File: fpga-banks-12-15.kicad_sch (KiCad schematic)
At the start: 1 part, among them U1 XC7K410T-2FFG900I

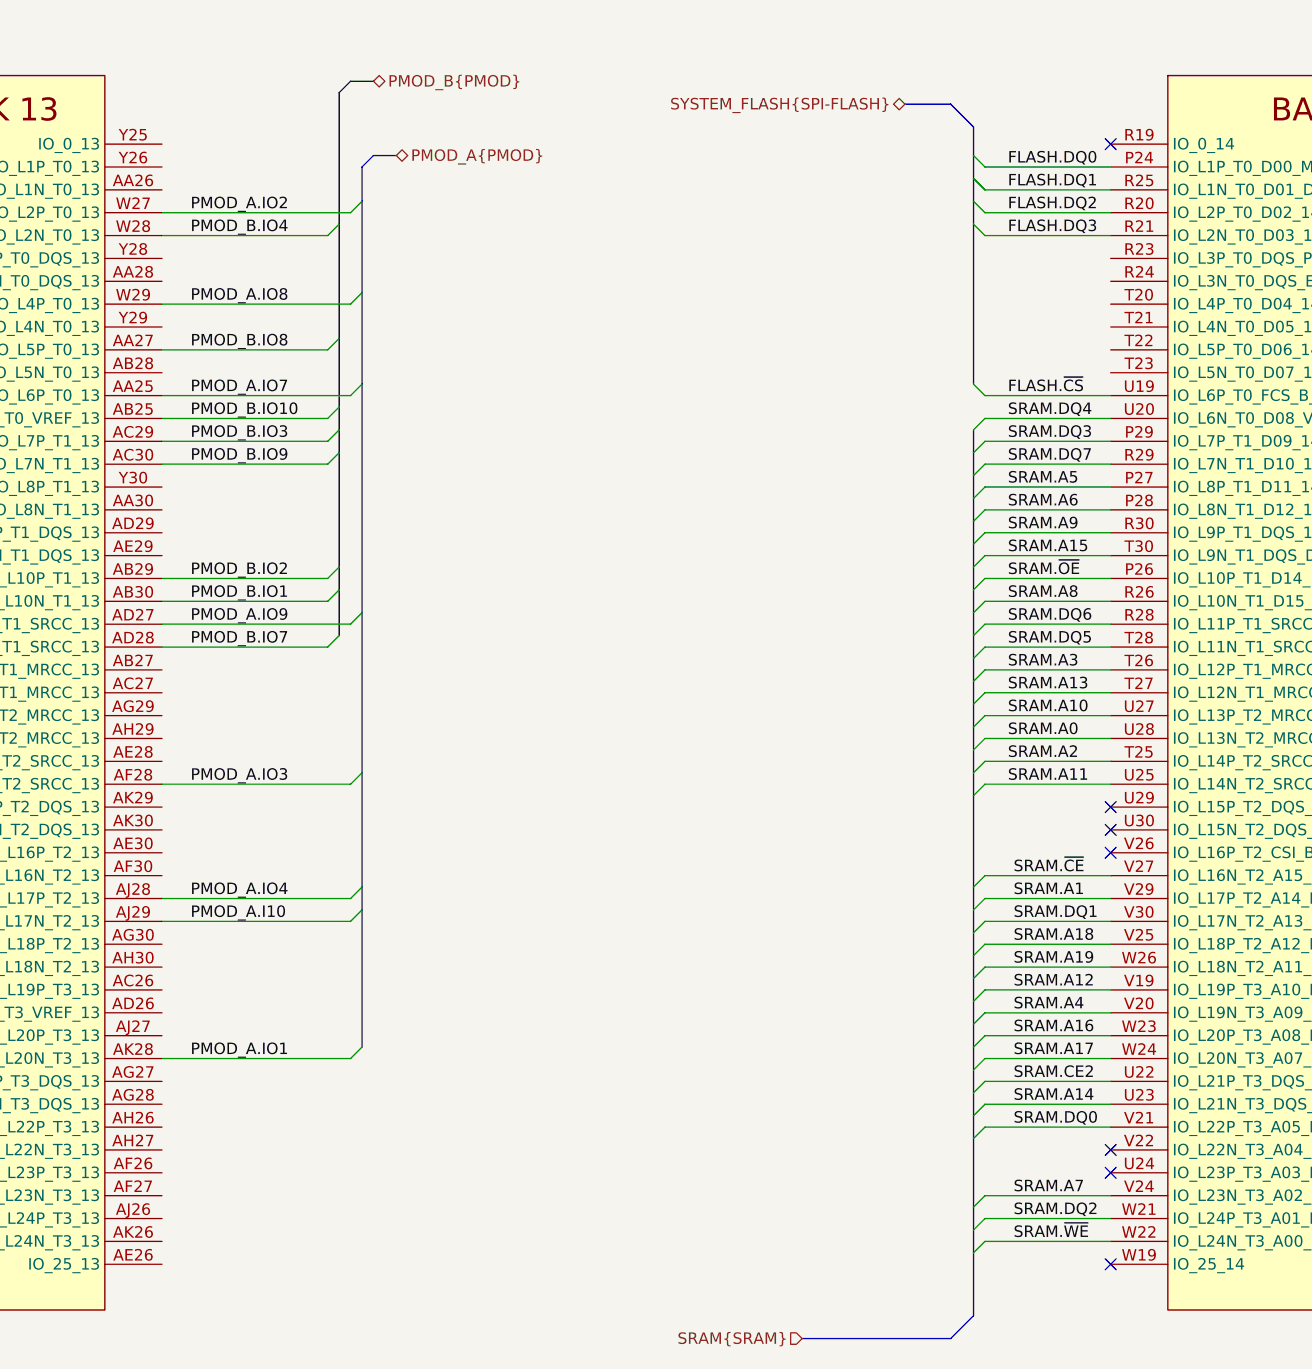
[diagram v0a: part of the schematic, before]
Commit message: Update system flash bus unfolded labels
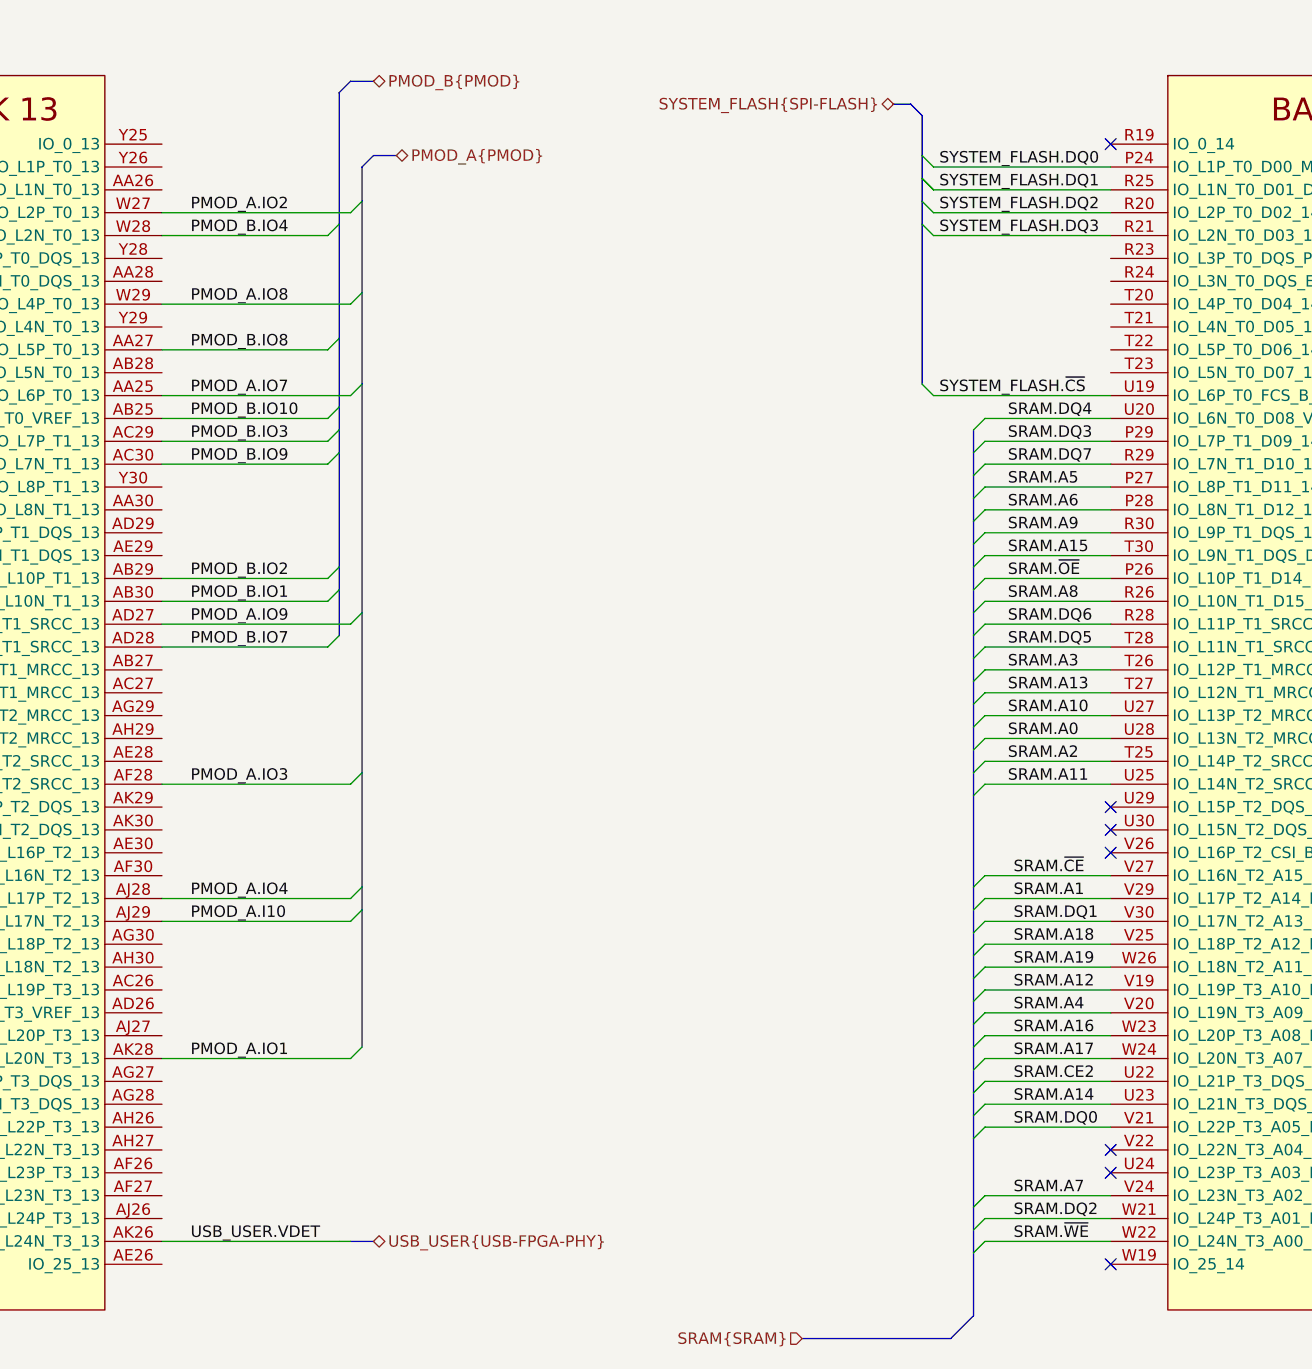
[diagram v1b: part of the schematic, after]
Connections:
- net USB_USER.VDET: now reaches U1.AK26 (IO_L24N_T3_13)
- net FLASH.DQ0 renamed SYSTEM_FLASH.DQ0
- net FLASH.DQ1 renamed SYSTEM_FLASH.DQ1
- net FLASH.DQ2 renamed SYSTEM_FLASH.DQ2
- net FLASH.DQ3 renamed SYSTEM_FLASH.DQ3
- net FLASH.~{CS} renamed SYSTEM_FLASH.~{CS}
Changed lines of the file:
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@@
     (stroke (width 0) (type default) (color 0 0 0 0))
   )
-  (bus_entry (at 240.03 80.01) (size 1.27 1.27)
+  (bus_entry (at 234.315 80.01) (size 1.27 1.27)
     (stroke (width 0) (type default) (color 0 0 0 0))
   )
@@
     (stroke (width 0) (type default) (color 0 0 0 0))
   )
-  (bus_entry (at 240.03 80.01) (size 1.27 1.27)
+  (bus_entry (at 234.315 80.01) (size 1.27 1.27)
     (stroke (width 0) (type default) (color 0 0 0 0))
   )
@@
     (stroke (width 0) (type default) (color 0 0 0 0))
   )
-  (bus_entry (at 240.03 102.87) (size 1.27 1.27)
-    (stroke (width 0) (type default) (color 0 0 0 0))
-  )
-  (bus_entry (at 240.03 77.47) (size 1.27 1.27)
+  (bus_entry (at 234.315 102.87) (size 1.27 1.27)
+    (stroke (width 0) (type default) (color 0 0 0 0))
+  )
+  (bus_entry (at 234.315 77.47) (size 1.27 1.27)
     (stroke (width 0) (type default) (color 0 0 0 0))
   )
@@
     (stroke (width 0) (type default) (color 0 0 0 0))
   )
-  (bus_entry (at 240.03 85.09) (size 1.27 1.27)
+  (bus_entry (at 234.315 85.09) (size 1.27 1.27)
     (stroke (width 0) (type default) (color 0 0 0 0))
   )
@@
     (stroke (width 0) (type default) (color 0 0 0 0))
   )
+  (bus_entry (at 169.545 198.12) (size 1.27 0)
+    (stroke (width 0) (type default) (color 0 0 0 0))
+  )
   (bus_entry (at 172.085 158.75) (size -1.27 1.27)
     (stroke (width 0) (type default) (color 0 0 0 0))
@@
     (stroke (width 0) (type default) (color 0 0 0 0))
   )
-  (bus_entry (at 240.03 82.55) (size 1.27 1.27)
+  (bus_entry (at 234.315 82.55) (size 1.27 1.27)
     (stroke (width 0) (type default) (color 0 0 0 0))
   )
@@
     (stroke (width 0) (type default) (color 0 0 0 0))
   )
-  (wire (pts (xy 241.3 78.74) (xy 255.27 78.74))
+  (wire (pts (xy 235.585 78.74) (xy 255.27 78.74))
     (stroke (width 0) (type default) (color 0 0 0 0))
   )
@@
     (stroke (width 0) (type default) (color 0 0 0 0))
   )
-  (bus (pts (xy 232.41 71.755) (xy 237.49 71.755))
-    (stroke (width 0) (type default) (color 0 0 0 0))
-  )
   (wire (pts (xy 241.3 139.7) (xy 255.27 139.7))
     (stroke (width 0) (type default) (color 0 0 0 0))
@@
     (stroke (width 0) (type default) (color 0 0 0 0))
   )
-  (bus (pts (xy 240.03 85.09) (xy 240.03 102.87))
+  (bus (pts (xy 234.315 85.09) (xy 234.315 102.87))
     (stroke (width 0) (type default) (color 0 0 0 0))
   )
@@
     (stroke (width 0) (type default) (color 0 0 0 0))
   )
-  (wire (pts (xy 241.3 104.14) (xy 255.27 104.14))
+  (wire (pts (xy 235.585 104.14) (xy 255.27 104.14))
     (stroke (width 0) (type default) (color 0 0 0 0))
   )
@@
     (stroke (width 0) (type default) (color 0 0 0 0))
   )
-  (wire (pts (xy 241.3 83.82) (xy 255.27 83.82))
+  (wire (pts (xy 235.585 83.82) (xy 255.27 83.82))
     (stroke (width 0) (type default) (color 0 0 0 0))
   )
@@
     (stroke (width 0) (type default) (color 0 0 0 0))
   )
-  (wire (pts (xy 241.3 86.36) (xy 255.27 86.36))
+  (wire (pts (xy 235.585 86.36) (xy 255.27 86.36))
     (stroke (width 0) (type default) (color 0 0 0 0))
   )
@@
     (stroke (width 0) (type default) (color 0 0 0 0))
   )
+  (bus (pts (xy 233.045 71.755) (xy 231.14 71.755))
+    (stroke (width 0) (type default) (color 0 0 0 0))
+  )
   (wire (pts (xy 241.3 127) (xy 255.27 127))
     (stroke (width 0) (type default) (color 0 0 0 0))
@@
     (stroke (width 0) (type default) (color 0 0 0 0))
   )
-  (bus (pts (xy 240.03 74.295) (xy 240.03 77.47))
+  (wire (pts (xy 169.545 198.12) (xy 149.86 198.12))
+    (stroke (width 0) (type default) (color 0 0 0 0))
+  )
+  (bus (pts (xy 234.315 73.025) (xy 234.315 77.47))
     (stroke (width 0) (type default) (color 0 0 0 0))
   )
@@
     (stroke (width 0) (type default) (color 0 0 0 0))
   )
-  (bus (pts (xy 237.49 71.755) (xy 240.03 74.295))
-    (stroke (width 0) (type default) (color 0 0 0 0))
-  )
   (bus (pts (xy 240.03 110.49) (xy 240.03 113.03))
     (stroke (width 0) (type default) (color 0 0 0 0))
@@
     (stroke (width 0) (type default) (color 0 0 0 0))
   )
+  (bus (pts (xy 234.315 73.025) (xy 233.045 71.755))
+    (stroke (width 0) (type default) (color 0 0 0 0))
+  )
   (bus (pts (xy 172.085 82.55) (xy 172.085 92.71))
     (stroke (width 0) (type default) (color 0 0 0 0))
@@
     (stroke (width 0) (type default) (color 0 0 0 0))
   )
-  (bus (pts (xy 240.03 77.47) (xy 240.03 80.01))
+  (bus (pts (xy 234.315 77.47) (xy 234.315 80.01))
     (stroke (width 0) (type default) (color 0 0 0 0))
   )
@@
     (stroke (width 0) (type default) (color 0 0 0 0))
   )
+  (bus (pts (xy 170.815 198.12) (xy 173.355 198.12))
+    (stroke (width 0) (type default) (color 0 0 0 0))
+  )
   (wire (pts (xy 149.86 109.22) (xy 168.275 109.22))
     (stroke (width 0) (type default) (color 0 0 0 0))
@@
     (stroke (width 0) (type default) (color 0 0 0 0))
   )
-  (wire (pts (xy 241.3 81.28) (xy 255.27 81.28))
+  (wire (pts (xy 235.585 81.28) (xy 255.27 81.28))
     (stroke (width 0) (type default) (color 0 0 0 0))
   )
@@
     (stroke (width 0) (type default) (color 0 0 0 0))
   )
-  (bus (pts (xy 240.03 80.01) (xy 240.03 82.55))
+  (bus (pts (xy 234.315 80.01) (xy 234.315 82.55))
     (stroke (width 0) (type default) (color 0 0 0 0))
   )
@@
     (stroke (width 0) (type default) (color 0 0 0 0))
   )
-  (bus (pts (xy 240.03 82.55) (xy 240.03 85.09))
+  (bus (pts (xy 234.315 82.55) (xy 234.315 85.09))
     (stroke (width 0) (type default) (color 0 0 0 0))
   )
@@
     (effects (font (size 1.27 1.27)) (justify left bottom))
   )
-  (label "FLASH.DQ0" (at 243.84 78.74 0)
+  (label "SYSTEM_FLASH.DQ0" (at 236.22 78.74 0)
     (effects (font (size 1.27 1.27)) (justify left bottom))
   )
@@
     (effects (font (size 1.27 1.27)) (justify left bottom))
   )
+  (label "USB_USER.VDET" (at 153.035 198.12 0)
+    (effects (font (size 1.27 1.27)) (justify left bottom))
+  )
   (label "SRAM.DQ3" (at 243.84 109.22 0)
     (effects (font (size 1.27 1.27)) (justify left bottom))
   )
-  (label "FLASH.DQ2" (at 243.84 83.82 0)
+  (label "SYSTEM_FLASH.DQ2" (at 236.22 83.82 0)
     (effects (font (size 1.27 1.27)) (justify left bottom))
   )
@@
     (effects (font (size 1.27 1.27)) (justify left bottom))
   )
-  (label "FLASH.~{CS}" (at 243.84 104.14 0)
+  (label "SYSTEM_FLASH.~{CS}" (at 236.22 104.14 0)
     (effects (font (size 1.27 1.27)) (justify left bottom))
   )
@@
     (effects (font (size 1.27 1.27)) (justify left bottom))
   )
-  (label "FLASH.DQ1" (at 243.84 81.28 0)
+  (label "SYSTEM_FLASH.DQ1" (at 236.22 81.28 0)
     (effects (font (size 1.27 1.27)) (justify left bottom))
   )
@@
     (effects (font (size 1.27 1.27)) (justify left bottom))
   )
-  (label "FLASH.DQ3" (at 243.84 86.36 0)
+  (label "SYSTEM_FLASH.DQ3" (at 236.22 86.36 0)
     (effects (font (size 1.27 1.27)) (justify left bottom))
   )
@@
     (effects (font (size 1.27 1.27)) (justify left bottom))
   )
-  (hierarchical_label "SYSTEM_FLASH{SPI-FLASH}" (shape bidirectional) (at 232.41 71.755 180)
+  (hierarchical_label "USB_USER{USB-FPGA-PHY}" (shape bidirectional) (at 173.355 198.12 0)
+    (effects (font (size 1.27 1.27)) (justify left))
+  )
+  (hierarchical_label "SYSTEM_FLASH{SPI-FLASH}" (shape bidirectional) (at 231.14 71.755 180)
     (effects (font (size 1.27 1.27)) (justify right))
   )

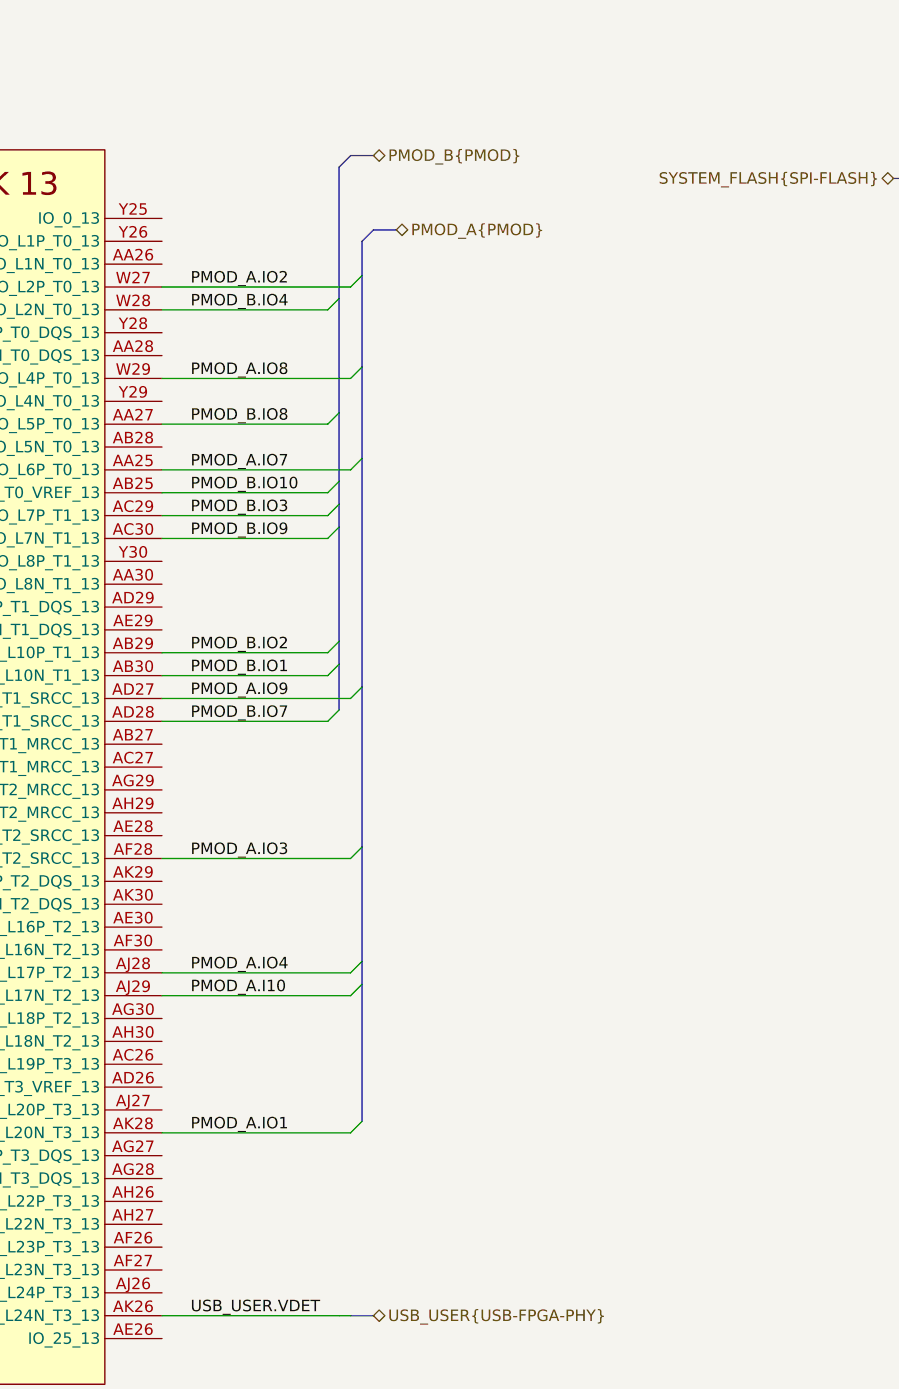
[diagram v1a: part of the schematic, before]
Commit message: Connect LED, DIP switch and buttons to FPGA
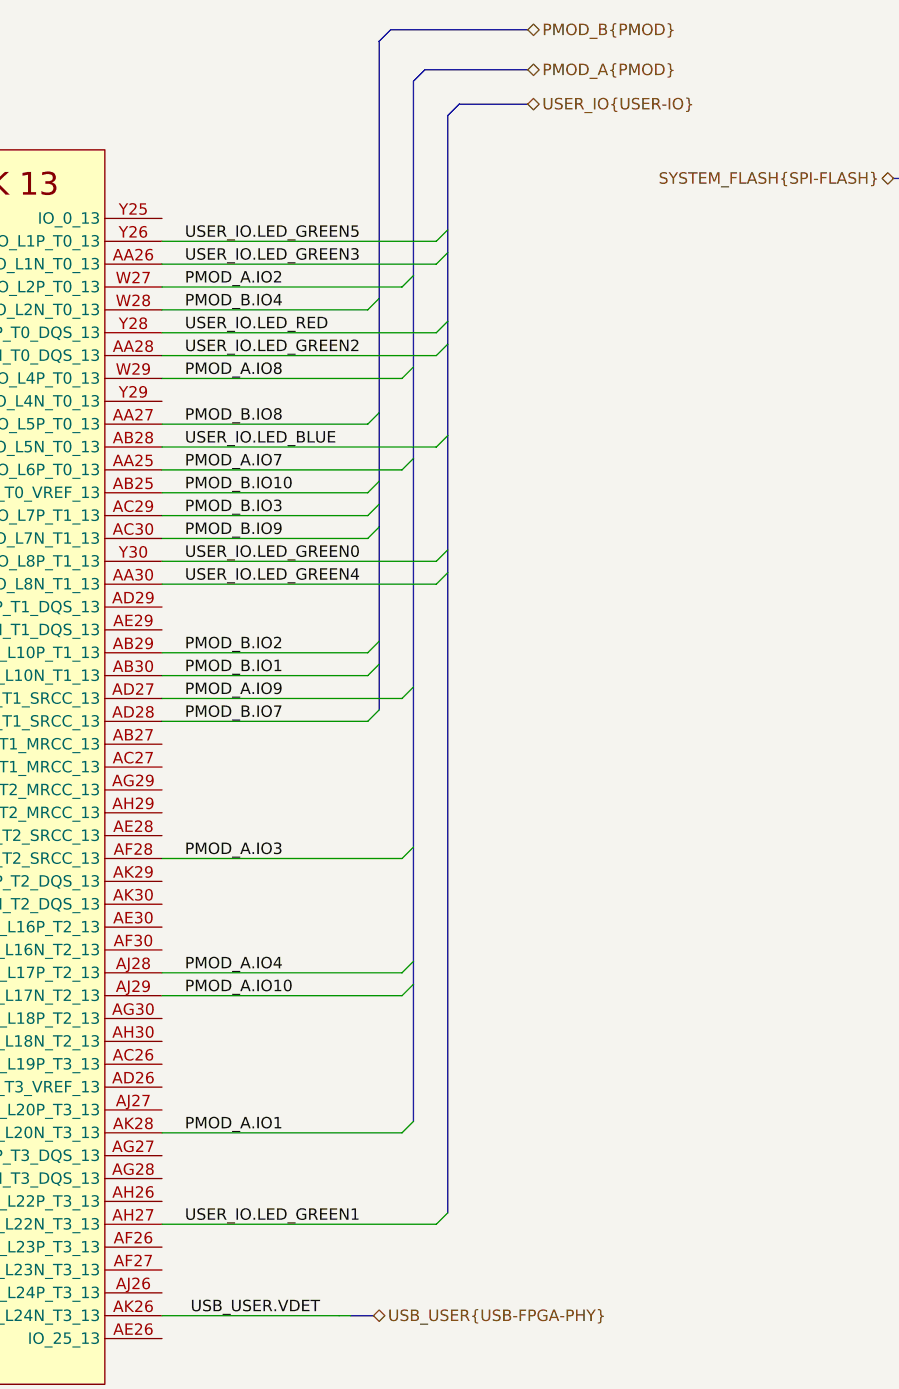
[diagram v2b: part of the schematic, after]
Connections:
- net USER_IO.LED_GREEN3: now reaches U1.AA26 (IO_L1N_T0_13)
- net USER_IO.LED_GREEN2: now reaches U1.AA28 (IO_L3N_T0_DQS_13)
- net USER_IO.LED_GREEN4: now reaches U1.AA30 (IO_L8N_T1_13)
- net USER_IO.LED_BLUE: now reaches U1.AB28 (IO_L5N_T0_13)
- net USER_IO.LED_GREEN1: now reaches U1.AH27 (IO_L22N_T3_13)
- net USER_IO.LED_GREEN5: now reaches U1.Y26 (IO_L1P_T0_13)
- net USER_IO.LED_RED: now reaches U1.Y28 (IO_L3P_T0_DQS_13)
- net USER_IO.LED_GREEN0: now reaches U1.Y30 (IO_L8P_T1_13)
- net PMOD_A.I10 renamed PMOD_A.IO10
